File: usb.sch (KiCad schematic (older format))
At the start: 102 parts, among them J201 USB_B, J202 CONN_ICSP, J203 CONN_MRESET, J204 CONN_LED, Q201 MMBT3904, Q202 MMBT3904, SW201 SW_RESET, U201 ATmega32U4-AU, U202 MAX7221, Y201 16M, Y202 16M

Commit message: Turning sockets upside-down and switching to SMD leds
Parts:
- LD0:0, LD0:1, LD0:2, LD0:3, LD0:4, LD0:5, LD0:6, LD0:7, LD1:0, LD1:1, LD1:2, LD1:3, LD1:4, LD1:5, LD1:6, LD1A:7, LD1B:7, LD2:0, LD2:1, LD2:2, LD2:3, LD2:4, LD2:5, LD2:6, LD2:7, LD3:0, LD3:1, LD3:2, LD3:3, LD3:4, LD3:5, LD3:6, LD3:7, LD4:0, LD4:1, LD4:2, LD4:3, LD4:4, LD4:5, LD4:6, LD4:7, LD5:0, LD5:1, LD5:2, LD5:3, LD5:4, LD5:5, LD5:6, LD5:7, LD6:0, LD6:1, LD6:2, LD6:3, LD6:4, LD6:5, LD6:6, LD6:7, LD7:0, LD7:1, LD7:2, LD7:3, LD7:5, LD7:6, LD7:7, LD7A:4, LD7B:4, LD7C:4: footprint LED_THT:LED_D3.0mm -> Mechboard16:LED_MX_6028R

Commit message: -30
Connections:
- net soft_i2c_scl: now reaches U201.32 (PC7)
- net soft_i2c_sda: now reaches U201.33 (~HWB~/PE2)
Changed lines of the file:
@@
 Sheet 2 2
 Title "Mechboard16"
-Date "2023-11-28"
+Date "2025-12-21"
 Rev "1git"
 Comp "SukkoPera"
@@
 Text Label 3830 3075 2    50   ~ 0
 ~mreset
-NoConn ~ 3310 4275
 NoConn ~ 3310 4375
 $Comp
@@
 	0    1    -1   0
 $EndComp
-NoConn ~ 3310 3175
 Text Label 3830 4775 2    50   ~ 0
 st_le_b
@@
 	1    0    0    -1
 $EndComp
+Wire Wire Line
+	3310 4275 3830 4275
+Text Label 3830 4275 2    50   ~ 0
+soft_i2c_sda
+Wire Wire Line
+	3310 3175 3830 3175
+NoConn ~ 3830 4275
+NoConn ~ 3830 3175
 Wire Bus Line
 	3930 2075 3930 2775
 Wire Bus Line
 	3930 3275 3930 3975
+Text Label 3830 3175 2    50   ~ 0
+soft_i2c_scl
 $EndSCHEMATC

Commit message: Add clock generator circuit
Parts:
- added C5, C6: 470n, Capacitor_SMD:C_0805_2012Metric_Pad1.18x1.45mm_HandSolder, symbol Device:CP1
- added C7, C8: 10u, Capacitor_THT:CP_Radial_D5.0mm_P2.00mm, symbol Device:CP1
- added CN3: CONN_CLOCK, Connector_PinHeader_2.54mm:PinHeader_1x06_P2.54mm_Vertical, symbol Connector:Conn_01x06_Male
- added Q1, Q2: BSS138, Package_TO_SOT_SMD:SOT-23, symbol Transistor_FET:BSS138
- added R5, R6, R7, R8: 10k, Resistor_SMD:R_0805_2012Metric_Pad1.20x1.40mm_HandSolder, symbol Device:R
- added U3: Si5351A-B-GT, Package_SO:MSOP-10_3x3mm_P0.5mm, symbol Oscillator:Si5351A-B-GT
- added U4: RT9193, Package_TO_SOT_SMD:SOT-23-5, symbol Regulator_Linear:TC1017-xCT
- added Y1: 25M, Crystal:Crystal_SMD_3225-4Pin_3.2x2.5mm, symbol Device:Crystal_GND24
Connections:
- net +5V: now also C7.1, R5.1, R6.1, U4.1 (VIN), U4.3 (~SHDN)
- net GND: now also C5.2, C6.2, C7.2, C8.2, CN3.1 (Pin_1), CN3.3 (Pin_3), CN3.5 (Pin_5), U3.8 (GND), U4.2 (GND), Y1.2, Y1.4
- net soft_i2c_scl: now also Q2.3 (D), R5.2
- net soft_i2c_sda: now also Q1.3 (D), R6.2
- new net: U3.2 (XA), Y1.1
- new net: U3.3 (XB), Y1.3
- new net +3V3: C5.1, C6.1, C8.1, Q1.1 (G), Q2.1 (G), R7.1, R8.1, U3.1 (VDD), U3.7 (VDDO), U4.5 (VOUT)
- new net clk0: CN3.2 (Pin_2), U3.10 (CLK0)
- new net clk1: CN3.4 (Pin_4), U3.9 (CLK1)
- new net clk2: CN3.6 (Pin_6), U3.6 (CLK2)
- new net scl_3v: Q2.2 (S), R7.2, U3.4 (SCL)
- new net sda_3v: Q1.2 (S), R8.2, U3.5 (SDA)
- no-connect marks 5 -> 3
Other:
- note added: "CLOCK GENERATOR"
- note added: "Y1: Must be 6, 8 or 10pF\nUse ABM8G-25.000MHZ-4Y-T3\nor ABM8G-25.000MHZ-B4Y-T"

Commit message: Some THT components -> SMD
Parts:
- C204: footprint Capacitor_THT:CP_Radial_D5.0mm_P2.00mm -> Capacitor_SMD:C_1206_3216Metric_Pad1.33x1.80mm_HandSolder; LCSC (none) -> C1848
- D201: footprint Diode_SMD:D_SMA -> Diode_SMD:D_SOD-323_HandSoldering
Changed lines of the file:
@@
 F 0 "D201" H 6880 3660 50  0000 C CNN
 F 1 "1n5819" H 6880 3691 50  0001 C CNN
-F 2 "Diode_SMD:D_SMA" H 6880 3565 50  0001 C CNN
+F 2 "Diode_SMD:D_SOD-323_HandSoldering" H 6880 3565 50  0001 C CNN
 F 3 "~" H 6880 3565 50  0001 C CNN
 F 4 "C191023" H 6880 3565 50  0001 C CNN "LCSC"
@@
 F 0 "C204" H 1900 3816 50  0000 L CNN
 F 1 "1u" H 1900 3725 50  0000 L CNN
-F 2 "Capacitor_THT:CP_Radial_D5.0mm_P2.00mm" H 1785 3770 50  0001 C CNN
+F 2 "Capacitor_SMD:C_1206_3216Metric_Pad1.33x1.80mm_HandSolder" H 1785 3770 50  0001 C CNN
 F 3 "~" H 1785 3770 50  0001 C CNN
+F 4 "C1848" H 1785 3770 50  0001 C CNN "LCSC"
 	1    1785 3770
 	1    0    0    -1
@@
 Text Label 1395 8525 0    50   ~ 0
 soft_i2c_scl
-Wire Bus Line
-	3930 3275 3930 3975
-Wire Bus Line
-	3930 2075 3930 2775
 Text Label 4245 9850 0    50   ~ 0
 clk0
@@
 Wire Wire Line
 	4845 9850 4245 9850
+Wire Bus Line
+	3930 2075 3930 2775
+Wire Bus Line
+	3930 3275 3930 3975
 $EndSCHEMATC

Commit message: Preparing for PCBA
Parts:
- C5, C6: LCSC (none) -> C13967
- D201: value 1n5819 -> 1n4148; LCSC C191023 -> C2128
- J202: LCSC (none) -> -
- LD0:0, LD0:1, LD0:2, LD0:3, LD0:4, LD0:5, LD0:6, LD0:7, LD1:0, LD1:1, LD1:2, LD1:3, LD1:4, LD1:5, LD1:6, LD1A:7, LD1B:7, LD2:0, LD2:1, LD2:2, LD2:3, LD2:4, LD2:5, LD2:6, LD2:7, LD3:0, LD3:1, LD3:2, LD3:3, LD3:4, LD3:5, LD3:6, LD3:7, LD4:0, LD4:1, LD4:2, LD4:3, LD4:4, LD4:5, LD4:6, LD4:7, LD5:0, LD5:1, LD5:2, LD5:3, LD5:4, LD5:5, LD5:6, LD5:7, LD6:0, LD6:1, LD6:2, LD6:3, LD6:4, LD6:5, LD6:6, LD6:7, LD7:0, LD7:1, LD7:2, LD7:3, LD7:5, LD7:6, LD7:7, LD7A:4, LD7B:4, LD7C:4: LCSC (none) -> C3646964
- Q1, Q2: LCSC (none) -> C75547
- R5, R6, R7, R8: LCSC (none) -> C17414
- Y1: LCSC (none) -> C596913

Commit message: Add ROM switcher
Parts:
- added CN4: CONN_ROMSWITCH, Connector_PinHeader_2.54mm:PinHeader_1x03_P2.54mm_Vertical, symbol Connector:Conn_01x03_Male
- added R5: 10k, Resistor_SMD:R_0805_2012Metric_Pad1.20x1.40mm_HandSolder, symbol Device:R
- added U1: 4066, Package_SO:SOIC-14_3.9x8.7mm_P1.27mm, symbol 4xxx:4066
- renumbered R5 to R6, R6 to R7, R7 to R8, R8 to R9
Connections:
- net +5V: now also R5.2
- net GND: now also U1.4
- net ROM_SWITCH: now reaches U201.1 (PE6)
- net ROM_SWITCH: now also U1.5, U1.6
- new net: CN4.2 (Pin_2), U1.11, U1.8
- new net: CN4.3 (Pin_3), U1.9
- new net: CN4.1 (Pin_1), U1.10
- new net ~switch: R5.1, U1.12, U1.3
- no-connect marks 3 -> 2
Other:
- note added: "H"
- note added: "Input and output are connected\nwhen enable is HIGH, so this\nworks essentially as an inverter"
- note added: "L"
- note added: "ROM SWITCHER"
- moved on the sheet: C5, C6, CN3, Q1, Q2, R6, R7, R8, R9, U3, Y1

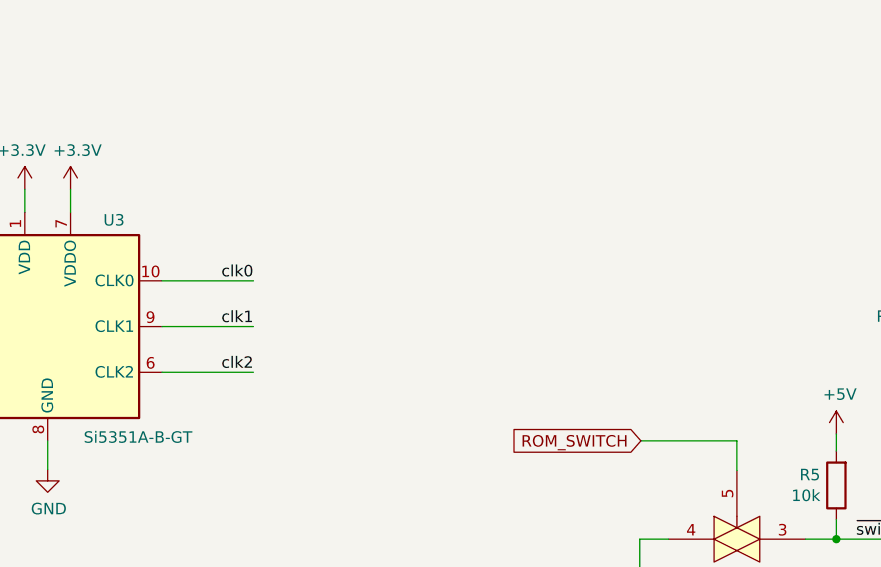
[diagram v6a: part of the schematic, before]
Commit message: Add series resistors on clock outputs
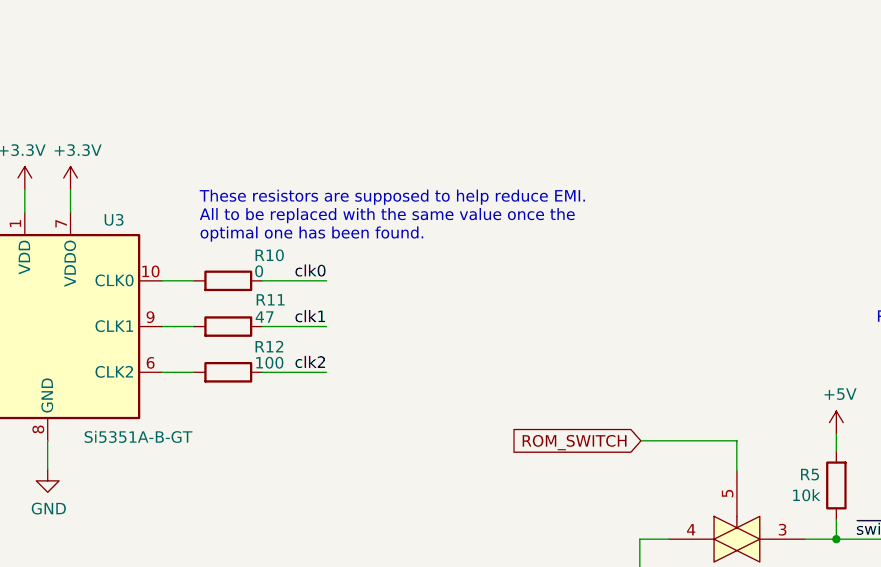
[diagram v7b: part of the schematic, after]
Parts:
- added R10: 0, Resistor_SMD:R_0805_2012Metric_Pad1.20x1.40mm_HandSolder, symbol Device:R
- added R11: 47, Resistor_SMD:R_0805_2012Metric_Pad1.20x1.40mm_HandSolder, symbol Device:R
- added R12: 100, Resistor_SMD:R_0805_2012Metric_Pad1.20x1.40mm_HandSolder, symbol Device:R
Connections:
- net clk0: now also R10.1; no longer U3.10 (CLK0)
- net clk1: now also R11.1; no longer U3.9 (CLK1)
- net clk2: now also R12.1; no longer U3.6 (CLK2)
- new net: R10.2, U3.10 (CLK0)
- new net: R12.2, U3.6 (CLK2)
- new net: R11.2, U3.9 (CLK1)
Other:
- note added: "These resistors are supposed to help reduce EMI.\nAll to be replaced with the same value once the\noptimal one has been found."
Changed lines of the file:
@@
 	2795 10240 2795 10345
 Wire Wire Line
-	6445 8430 6845 8430
-Text Label 6845 8430 2    50   ~ 0
+	6445 8430 6585 8430
+Text Label 7165 8430 2    50   ~ 0
 clk2
 Wire Wire Line
-	6445 8230 6845 8230
-Text Label 6845 8230 2    50   ~ 0
+	6445 8230 6585 8230
+Text Label 7165 8230 2    50   ~ 0
 clk1
 Wire Wire Line
-	6445 8030 6845 8030
-Text Label 6845 8030 2    50   ~ 0
+	6445 8030 6585 8030
+Text Label 7165 8030 2    50   ~ 0
 clk0
 Wire Wire Line
@@
 Text Notes 9570 8225 0    50   ~ 0
 ROM SWITCHER
+$Comp
+L Device:R R?
+U 1 1 6B453E72
+P 6735 8030
+AR Path="/656CF65E/695AAD16/6B453E72" Ref="R?"  Part="1"
+AR Path="/656CF65E/6B453E72" Ref="R10"  Part="1"
+F 0 "R10" V 6845 8210 50  0000 C CNN
+F 1 "0" V 6775 8165 50  0000 C CNN
+F 2 "Resistor_SMD:R_0805_2012Metric_Pad1.20x1.40mm_HandSolder" V 6665 8030 50  0001 C CNN
+F 3 "~" H 6735 8030 50  0001 C CNN
+F 4 "C17477" H 6735 8030 50  0001 C CNN "LCSC"
+	1    6735 8030
+	0    1    -1   0
+$EndComp
+$Comp
+L Device:R R?
+U 1 1 6B455C6D
+P 6735 8230
+AR Path="/656CF65E/695AAD16/6B455C6D" Ref="R?"  Part="1"
+AR Path="/656CF65E/6B455C6D" Ref="R11"  Part="1"
+F 0 "R11" V 6850 8415 50  0000 C CNN
+F 1 "47" V 6775 8390 50  0000 C CNN
+F 2 "Resistor_SMD:R_0805_2012Metric_Pad1.20x1.40mm_HandSolder" V 6665 8230 50  0001 C CNN
+F 3 "~" H 6735 8230 50  0001 C CNN
+F 4 "C17714" H 6735 8230 50  0001 C CNN "LCSC"
+	1    6735 8230
+	0    1    -1   0
+$EndComp
+$Comp
+L Device:R R?
+U 1 1 6B4562F2
+P 6735 8430
+AR Path="/656CF65E/695AAD16/6B4562F2" Ref="R?"  Part="1"
+AR Path="/656CF65E/6B4562F2" Ref="R12"  Part="1"
+F 0 "R12" V 6845 8610 50  0000 C CNN
+F 1 "100" V 6775 8610 50  0000 C CNN
+F 2 "Resistor_SMD:R_0805_2012Metric_Pad1.20x1.40mm_HandSolder" V 6665 8430 50  0001 C CNN
+F 3 "~" H 6735 8430 50  0001 C CNN
+F 4 "C17408" H 6735 8430 50  0001 C CNN "LCSC"
+	1    6735 8430
+	0    1    -1   0
+$EndComp
+Wire Wire Line
+	6885 8030 7165 8030
+Wire Wire Line
+	6885 8230 7165 8230
+Wire Wire Line
+	6885 8430 7165 8430
 Wire Bus Line
 	3930 2075 3930 2775
 Wire Bus Line
 	3930 3275 3930 3975
+Text Notes 6610 7860 0    50   ~ 0
+These resistors are supposed to help reduce EMI.\nAll to be replaced with the same value once the\noptimal one has been found.
 $EndSCHEMATC
